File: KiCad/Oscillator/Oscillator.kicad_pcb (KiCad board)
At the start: 2 copper layers, 78 x 75.5 mm, 51 parts, among them J1 Screw_Terminal_01x02, J2 Screw_Terminal_01x03, Q1 NPN, Q2 PNP, Q3 NPN, Q4 PNP, U1 40106, U2 TL074

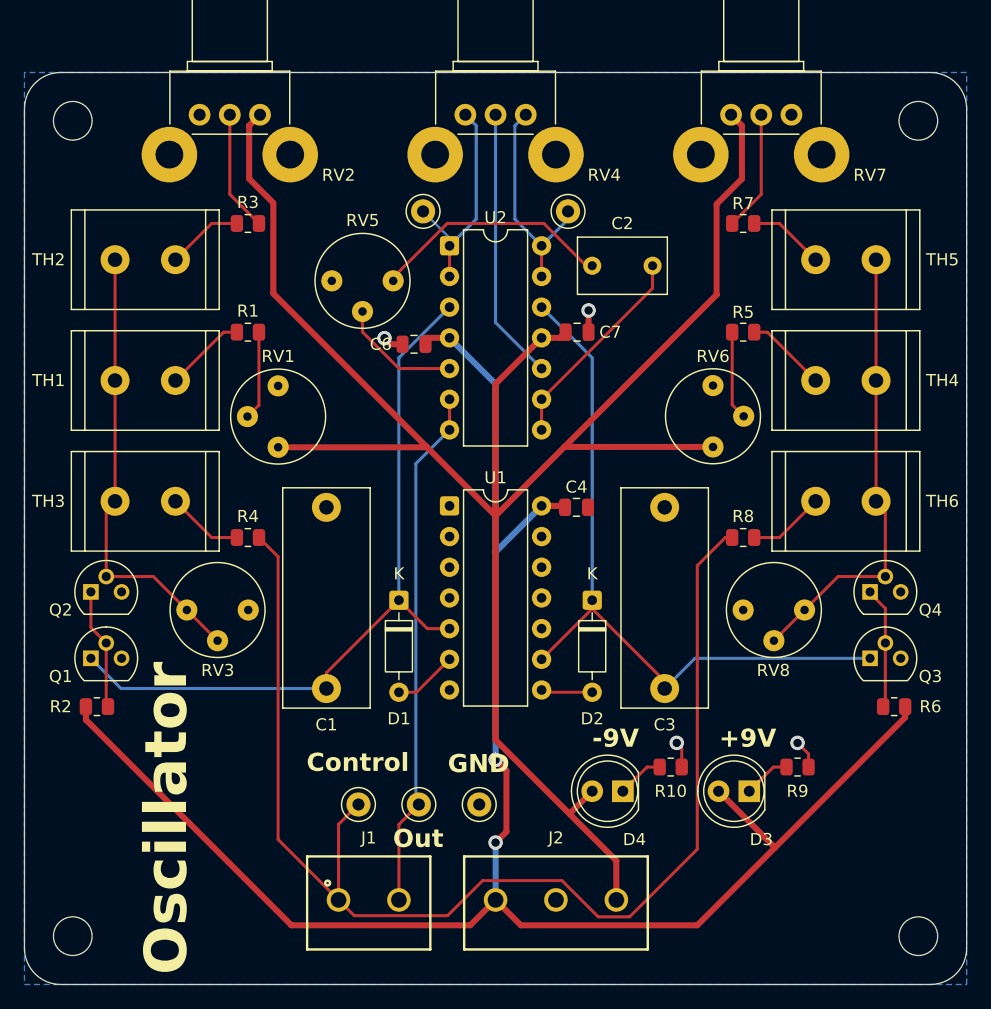
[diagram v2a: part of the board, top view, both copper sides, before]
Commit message: added mounting holes to schematics, adjusted board sizes
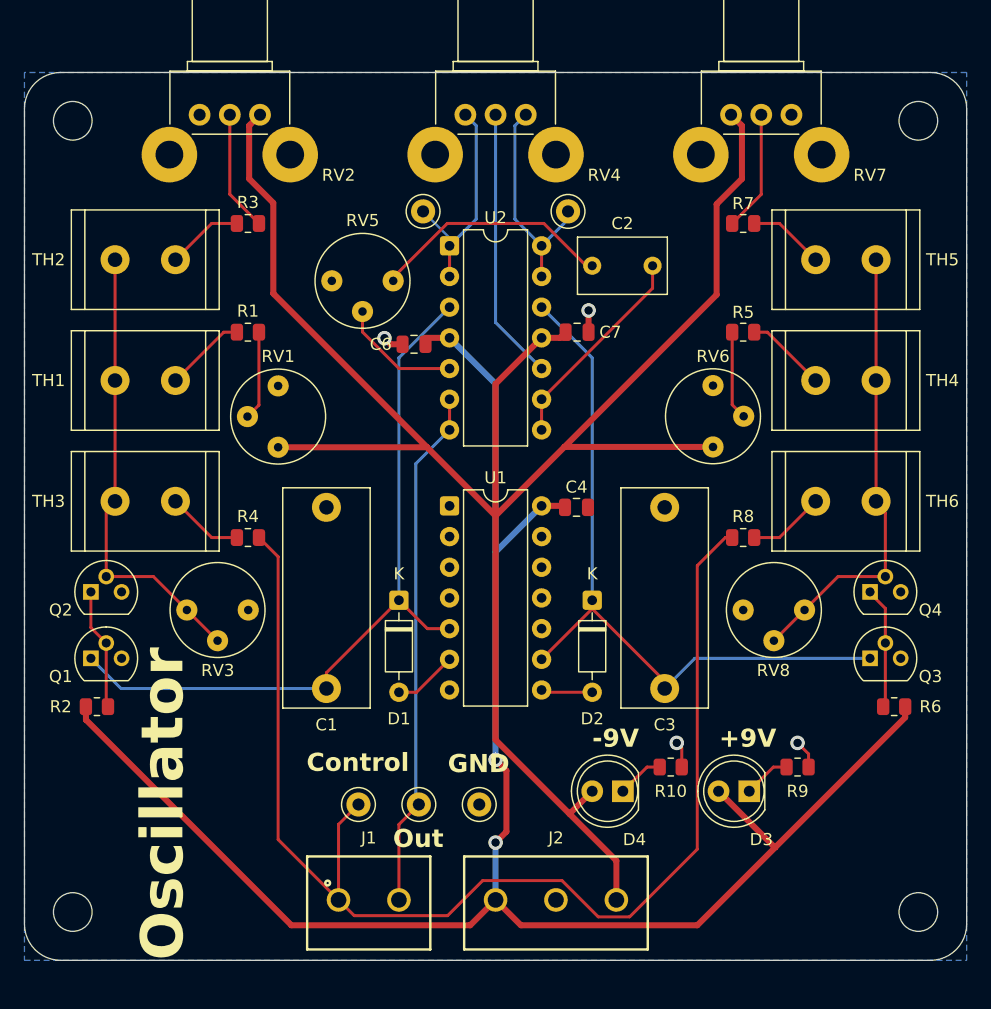
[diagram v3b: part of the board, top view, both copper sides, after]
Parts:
- moved H2 2.00 mm to (44.0, 105.0)
- moved H3 2.00 mm to (114.0, 105.0)
- renumbered REF** to H1, REF** to H2, REF** to H3, REF** to H4
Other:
- board size 78 x 75.5 mm -> 78 x 73.5 mm
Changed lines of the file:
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@@
 			(at 4.12 5.365 0)
 			(layer "F.Fab")
+			(hide yes)
 			(effects
 				(font
@@
 	(footprint "MountingHole:MountingHole_3.2mm_M3"
 		(layer "F.Cu")
-		(at 114 107)
+		(at 114 105)
 		(descr "Mounting Hole 3.2mm, M3, no annular, generated by kicad-footprint-generator mountinghole.py")
 		(tags "mountinghole M3")
-		(property "Reference" "REF**"
+		(property "Reference" "H3"
 			(at 0 -4.15 0)
 			(layer "F.SilkS")
@@
 		(descr "Mounting Hole 3.2mm, M3, no annular, generated by kicad-footprint-generator mountinghole.py")
 		(tags "mountinghole M3")
-		(property "Reference" "REF**"
+		(property "Reference" "H1"
 			(at 0 -4.15 0)
 			(layer "F.SilkS")
@@
 		(descr "Mounting Hole 3.2mm, M3, no annular, generated by kicad-footprint-generator mountinghole.py")
 		(tags "mountinghole M3")
-		(property "Reference" "REF**"
+		(property "Reference" "H4"
 			(at 0 -4.15 0)
 			(layer "F.SilkS")
@@
 	(footprint "MountingHole:MountingHole_3.2mm_M3"
 		(layer "F.Cu")
-		(at 44 107)
+		(at 44 105)
 		(descr "Mounting Hole 3.2mm, M3, no annular, generated by kicad-footprint-generator mountinghole.py")
 		(tags "mountinghole M3")
-		(property "Reference" "REF**"
+		(property "Reference" "H2"
 			(at 0 -4.15 0)
 			(layer "F.SilkS")
@@
 			(at 4.12 5.365 0)
 			(layer "F.Fab")
+			(hide yes)
 			(effects
 				(font
@@
 	)
 	(gr_line
-		(start 40 108)
+		(start 40 106)
 		(end 40.000005 38.500006)
 		(stroke
@@
 	)
 	(gr_arc
-		(start 43 111)
-		(mid 40.87868 110.12132)
-		(end 40 108)
+		(start 43 109)
+		(mid 40.87868 108.12132)
+		(end 40 106)
 		(stroke
 			(width 0.05)
@@
 	)
 	(gr_line
-		(start 115 111)
-		(end 43 111)
+		(start 115 109)
+		(end 43 109)
 		(stroke
 			(width 0.05)
@@
 	)
 	(gr_arc
-		(start 117.999959 107.999959)
-		(mid 117.121279 110.121279)
-		(end 114.999959 110.999959)
+		(start 117.999959 105.999959)
+		(mid 117.121279 108.121279)
+		(end 114.999959 108.999959)
 		(stroke
 			(width 0.05)
@@
 	)
 	(gr_line
-		(start 118 108)
+		(start 118 106)
 		(end 117.999999 38.500002)
 		(stroke
@@
 	)
 	(gr_text "Oscillator"
-		(at 53.8 110.2 90)
+		(at 53.5 109 90)
 		(layer "F.SilkS")
 		(effects
@@
 		(polygon
 			(pts
-				(xy 40 35.5) (xy 40 111) (xy 118 111) (xy 118 35.5)
+				(xy 40 35.5) (xy 40 109) (xy 118 109) (xy 118 35.5)
 			)
 		)
